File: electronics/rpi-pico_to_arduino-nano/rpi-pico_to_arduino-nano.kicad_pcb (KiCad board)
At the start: 2 copper layers, 2 parts, among them U1 Pico

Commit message: add some connections and comments
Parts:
- moved U1 2.62 mm to (153.7, 107.3)
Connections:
- A1 pad 1: unconnected-(A1-Pad1) -> /GPIO1
- A1 pad 10: unconnected-(A1-Pad10) -> /GPIO7
- A1 pad 11: unconnected-(A1-Pad11) -> /GPIO8
- A1 pad 12: unconnected-(A1-Pad12) -> /GPIO9
- A1 pad 13: unconnected-(A1-Pad13) -> /GPIO10
- A1 pad 14: unconnected-(A1-Pad14) -> /GPIO11
- A1 pad 15: unconnected-(A1-Pad15) -> /GPIO12
- A1 pad 16: unconnected-(A1-Pad16) -> /GPIO13
- A1 pad 19: unconnected-(A1-Pad19) -> /GPIO26_ADC0
- A1 pad 2: unconnected-(A1-Pad2) -> /GPIO0
- A1 pad 20: unconnected-(A1-Pad20) -> /GPIO27_ADC1
- A1 pad 21: unconnected-(A1-Pad21) -> /GPIO26_ADC0
- A1 pad 29: unconnected-(A1-Pad29) -> GND
- A1 pad 4: unconnected-(A1-Pad4) -> GND
- A1 pad 5: unconnected-(A1-Pad5) -> /GPIO2
- A1 pad 6: unconnected-(A1-Pad6) -> /GPIO3
- A1 pad 7: unconnected-(A1-Pad7) -> /GPIO4
- A1 pad 8: unconnected-(A1-Pad8) -> /GPIO5
- A1 pad 9: unconnected-(A1-Pad9) -> /GPIO6
- U1 pad 1: unconnected-(U1-Pad1) -> /GPIO0
- U1 pad 10: unconnected-(U1-Pad10) -> /GPIO7
- U1 pad 11: unconnected-(U1-Pad11) -> /GPIO8
- U1 pad 12: unconnected-(U1-Pad12) -> /GPIO9
- U1 pad 13: unconnected-(U1-Pad13) -> GND
- U1 pad 14: unconnected-(U1-Pad14) -> /GPIO10
- U1 pad 15: unconnected-(U1-Pad15) -> /GPIO11
- U1 pad 16: unconnected-(U1-Pad16) -> /GPIO12
- U1 pad 17: unconnected-(U1-Pad17) -> /GPIO13
- U1 pad 18: unconnected-(U1-Pad18) -> GND
- U1 pad 19: unconnected-(U1-Pad19) -> /GPIO14
- U1 pad 2: unconnected-(U1-Pad2) -> /GPIO1
- U1 pad 20: unconnected-(U1-Pad20) -> /GPIO15
- U1 pad 21: unconnected-(U1-Pad21) -> /GPIO16
- U1 pad 22: unconnected-(U1-Pad22) -> /GPIO17
- U1 pad 23: unconnected-(U1-Pad23) -> GND
- U1 pad 24: unconnected-(U1-Pad24) -> /GPIO18
- U1 pad 25: unconnected-(U1-Pad25) -> /GPIO19
- U1 pad 26: unconnected-(U1-Pad26) -> /GPIO20
- U1 pad 27: unconnected-(U1-Pad27) -> /GPIO21
- U1 pad 28: unconnected-(U1-Pad28) -> GND
- U1 pad 29: unconnected-(U1-Pad29) -> /GPIO22
- U1 pad 3: unconnected-(U1-Pad3) -> GND
- U1 pad 30: unconnected-(U1-Pad30) -> /RUN
- U1 pad 31: unconnected-(U1-Pad31) -> /GPIO26_ADC0
- U1 pad 32: unconnected-(U1-Pad32) -> /GPIO27_ADC1
- U1 pad 33: unconnected-(U1-Pad33) -> GND
- U1 pad 34: unconnected-(U1-Pad34) -> /GPIO28_ADC2
- U1 pad 35: unconnected-(U1-Pad35) -> /ADC_VREF
- U1 pad 36: unconnected-(U1-Pad36) -> /3V3
- U1 pad 37: unconnected-(U1-Pad37) -> /3V3_EN
- U1 pad 38: unconnected-(U1-Pad38) -> GND
- U1 pad 39: unconnected-(U1-Pad39) -> /VSYS
- U1 pad 4: unconnected-(U1-Pad4) -> /GPIO2
- U1 pad 40: unconnected-(U1-Pad40) -> /VBUS
- U1 pad 41: unconnected-(U1-Pad41) -> /SWCLK
- U1 pad 42: unconnected-(U1-Pad42) -> GND
- U1 pad 43: unconnected-(U1-Pad43) -> /SWDIO
- U1 pad 5: unconnected-(U1-Pad5) -> /GPIO3
- U1 pad 6: unconnected-(U1-Pad6) -> /GPIO4
- U1 pad 7: unconnected-(U1-Pad7) -> /GPIO5
- U1 pad 8: unconnected-(U1-Pad8) -> GND
- U1 pad 9: unconnected-(U1-Pad9) -> /GPIO6

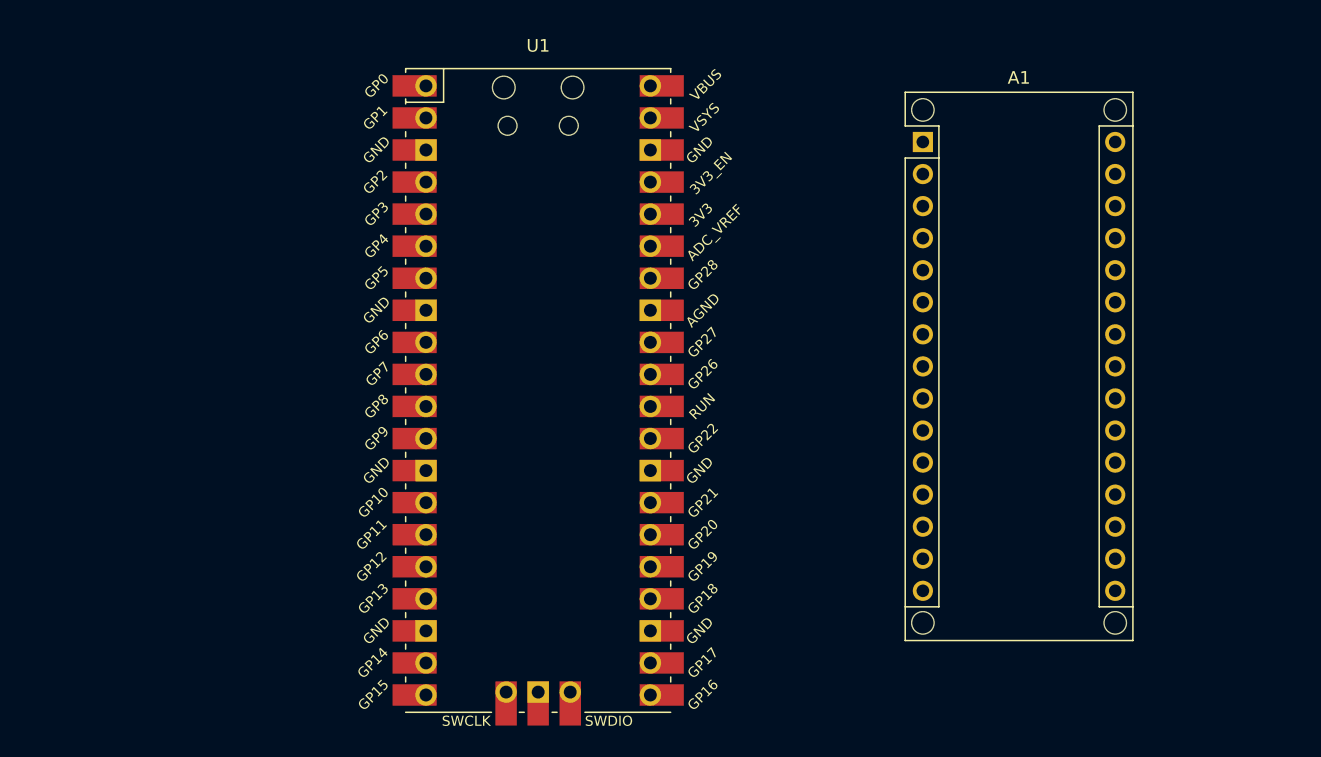
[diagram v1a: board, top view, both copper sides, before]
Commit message: add connection matrix
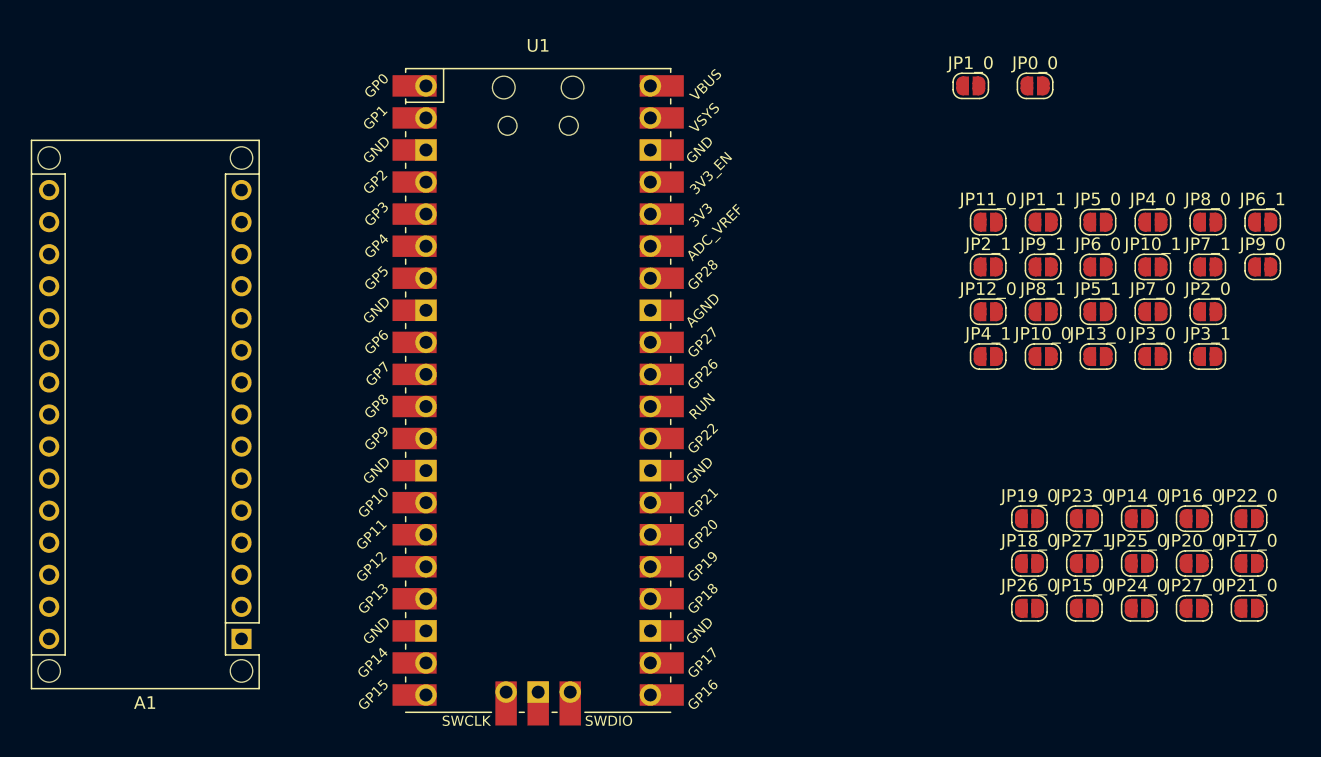
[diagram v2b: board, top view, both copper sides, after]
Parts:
- added JP0_0: SolderJumper_2_Open, Jumper:SolderJumper-2_P1.3mm_Open_RoundedPad1.0x1.5mm, F.Cu at (193.0, 83.2)
- added JP10_0: SolderJumper_2_Open, Jumper:SolderJumper-2_P1.3mm_Open_RoundedPad1.0x1.5mm, F.Cu at (193.7, 104.6)
- added JP10_1: SolderJumper_2_Open, Jumper:SolderJumper-2_P1.3mm_Open_RoundedPad1.0x1.5mm, F.Cu at (202.4, 97.5)
- added JP11_0: SolderJumper_2_Open, Jumper:SolderJumper-2_P1.3mm_Open_RoundedPad1.0x1.5mm, F.Cu at (189.3, 94.0)
- added JP12_0: SolderJumper_2_Open, Jumper:SolderJumper-2_P1.3mm_Open_RoundedPad1.0x1.5mm, F.Cu at (189.3, 101.1)
- added JP13_0: SolderJumper_2_Open, Jumper:SolderJumper-2_P1.3mm_Open_RoundedPad1.0x1.5mm, F.Cu at (198.0, 104.6)
- added JP14_0: SolderJumper_2_Open, Jumper:SolderJumper-2_P1.3mm_Open_RoundedPad1.0x1.5mm, F.Cu at (201.3, 117.5)
- added JP15_0: SolderJumper_2_Open, Jumper:SolderJumper-2_P1.3mm_Open_RoundedPad1.0x1.5mm, F.Cu at (196.9, 124.6)
- added JP16_0: SolderJumper_2_Open, Jumper:SolderJumper-2_P1.3mm_Open_RoundedPad1.0x1.5mm, F.Cu at (205.6, 117.5)
- added JP17_0: SolderJumper_2_Open, Jumper:SolderJumper-2_P1.3mm_Open_RoundedPad1.0x1.5mm, F.Cu at (210.0, 121.0)
- added JP18_0: SolderJumper_2_Open, Jumper:SolderJumper-2_P1.3mm_Open_RoundedPad1.0x1.5mm, F.Cu at (192.6, 121.0)
- added JP19_0: SolderJumper_2_Open, Jumper:SolderJumper-2_P1.3mm_Open_RoundedPad1.0x1.5mm, F.Cu at (192.6, 117.5)
- added JP1_0: SolderJumper_2_Open, Jumper:SolderJumper-2_P1.3mm_Open_RoundedPad1.0x1.5mm, F.Cu at (187.9, 83.2)
- added JP1_1: SolderJumper_2_Open, Jumper:SolderJumper-2_P1.3mm_Open_RoundedPad1.0x1.5mm, F.Cu at (193.7, 94.0)
- added JP20_0: SolderJumper_2_Open, Jumper:SolderJumper-2_P1.3mm_Open_RoundedPad1.0x1.5mm, F.Cu at (205.6, 121.0)
- added JP21_0: SolderJumper_2_Open, Jumper:SolderJumper-2_P1.3mm_Open_RoundedPad1.0x1.5mm, F.Cu at (210.0, 124.6)
- added JP22_0: SolderJumper_2_Open, Jumper:SolderJumper-2_P1.3mm_Open_RoundedPad1.0x1.5mm, F.Cu at (210.0, 117.5)
- added JP23_0: SolderJumper_2_Open, Jumper:SolderJumper-2_P1.3mm_Open_RoundedPad1.0x1.5mm, F.Cu at (196.9, 117.5)
- added JP24_0: SolderJumper_2_Open, Jumper:SolderJumper-2_P1.3mm_Open_RoundedPad1.0x1.5mm, F.Cu at (201.3, 124.6)
- added JP25_0: SolderJumper_2_Open, Jumper:SolderJumper-2_P1.3mm_Open_RoundedPad1.0x1.5mm, F.Cu at (201.3, 121.0)
- added JP26_0: SolderJumper_2_Open, Jumper:SolderJumper-2_P1.3mm_Open_RoundedPad1.0x1.5mm, F.Cu at (192.6, 124.6)
- added JP27_0: SolderJumper_2_Open, Jumper:SolderJumper-2_P1.3mm_Open_RoundedPad1.0x1.5mm, F.Cu at (205.6, 124.6)
- added JP27_1: SolderJumper_2_Open, Jumper:SolderJumper-2_P1.3mm_Open_RoundedPad1.0x1.5mm, F.Cu at (196.9, 121.0)
- added JP2_0: SolderJumper_2_Open, Jumper:SolderJumper-2_P1.3mm_Open_RoundedPad1.0x1.5mm, F.Cu at (206.7, 101.1)
- added JP2_1: SolderJumper_2_Open, Jumper:SolderJumper-2_P1.3mm_Open_RoundedPad1.0x1.5mm, F.Cu at (189.3, 97.5)
- added JP3_0: SolderJumper_2_Open, Jumper:SolderJumper-2_P1.3mm_Open_RoundedPad1.0x1.5mm, F.Cu at (202.4, 104.6)
- added JP3_1: SolderJumper_2_Open, Jumper:SolderJumper-2_P1.3mm_Open_RoundedPad1.0x1.5mm, F.Cu at (206.7, 104.6)
- added JP4_0: SolderJumper_2_Open, Jumper:SolderJumper-2_P1.3mm_Open_RoundedPad1.0x1.5mm, F.Cu at (202.4, 94.0)
- added JP4_1: SolderJumper_2_Open, Jumper:SolderJumper-2_P1.3mm_Open_RoundedPad1.0x1.5mm, F.Cu at (189.3, 104.6)
- added JP5_0: SolderJumper_2_Open, Jumper:SolderJumper-2_P1.3mm_Open_RoundedPad1.0x1.5mm, F.Cu at (198.0, 94.0)
- added JP5_1: SolderJumper_2_Open, Jumper:SolderJumper-2_P1.3mm_Open_RoundedPad1.0x1.5mm, F.Cu at (198.0, 101.1)
- added JP6_0: SolderJumper_2_Open, Jumper:SolderJumper-2_P1.3mm_Open_RoundedPad1.0x1.5mm, F.Cu at (198.0, 97.5)
- added JP6_1: SolderJumper_2_Open, Jumper:SolderJumper-2_P1.3mm_Open_RoundedPad1.0x1.5mm, F.Cu at (211.1, 94.0)
- added JP7_0: SolderJumper_2_Open, Jumper:SolderJumper-2_P1.3mm_Open_RoundedPad1.0x1.5mm, F.Cu at (202.4, 101.1)
- added JP7_1: SolderJumper_2_Open, Jumper:SolderJumper-2_P1.3mm_Open_RoundedPad1.0x1.5mm, F.Cu at (206.7, 97.5)
- added JP8_0: SolderJumper_2_Open, Jumper:SolderJumper-2_P1.3mm_Open_RoundedPad1.0x1.5mm, F.Cu at (206.7, 94.0)
- added JP8_1: SolderJumper_2_Open, Jumper:SolderJumper-2_P1.3mm_Open_RoundedPad1.0x1.5mm, F.Cu at (193.7, 101.1)
- added JP9_0: SolderJumper_2_Open, Jumper:SolderJumper-2_P1.3mm_Open_RoundedPad1.0x1.5mm, F.Cu at (211.1, 97.5)
- added JP9_1: SolderJumper_2_Open, Jumper:SolderJumper-2_P1.3mm_Open_RoundedPad1.0x1.5mm, F.Cu at (193.7, 97.5)
- moved A1 66.8 mm to (130.2, 127.0), turned to 180 degrees
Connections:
- A1 pad 1: /GPIO1 -> /D1/TX
- A1 pad 10: /GPIO7 -> /D7
- A1 pad 11: /GPIO8 -> /D8
- A1 pad 12: /GPIO9 -> /D9
- A1 pad 13: /GPIO10 -> /D10
- A1 pad 14: /GPIO11 -> /D11
- A1 pad 15: /GPIO12 -> /D12
- A1 pad 16: /GPIO13 -> /D13
- A1 pad 17: unconnected-(A1-Pad17) -> /3V3
- A1 pad 18: unconnected-(A1-Pad18) -> /AREF
- A1 pad 19: /GPIO26_ADC0 -> /A0
- A1 pad 2: /GPIO0 -> /DO/RX
- A1 pad 20: /GPIO27_ADC1 -> /A1
- A1 pad 21: /GPIO26_ADC0 -> /A2
- A1 pad 22: unconnected-(A1-Pad22) -> /A3
- A1 pad 23: unconnected-(A1-Pad23) -> /A4
- A1 pad 24: unconnected-(A1-Pad24) -> /A5
- A1 pad 25: unconnected-(A1-Pad25) -> /A6
- A1 pad 26: unconnected-(A1-Pad26) -> /A7
- A1 pad 27: unconnected-(A1-Pad27) -> /+5V
- A1 pad 28: unconnected-(A1-Pad28) -> /~{RESET}
- A1 pad 3: unconnected-(A1-Pad3) -> /~{RESET}
- A1 pad 30: unconnected-(A1-Pad30) -> /VIN
- A1 pad 5: /GPIO2 -> /D2
- A1 pad 6: /GPIO3 -> /D3
- A1 pad 7: /GPIO4 -> /D4
- A1 pad 8: /GPIO5 -> /D5
- A1 pad 9: /GPIO6 -> /D6
- U1 pad 33: GND -> /AGND
- U1 pad 37: /3V3_EN -> unconnected-(U1-Pad37)

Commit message: place components on pcb
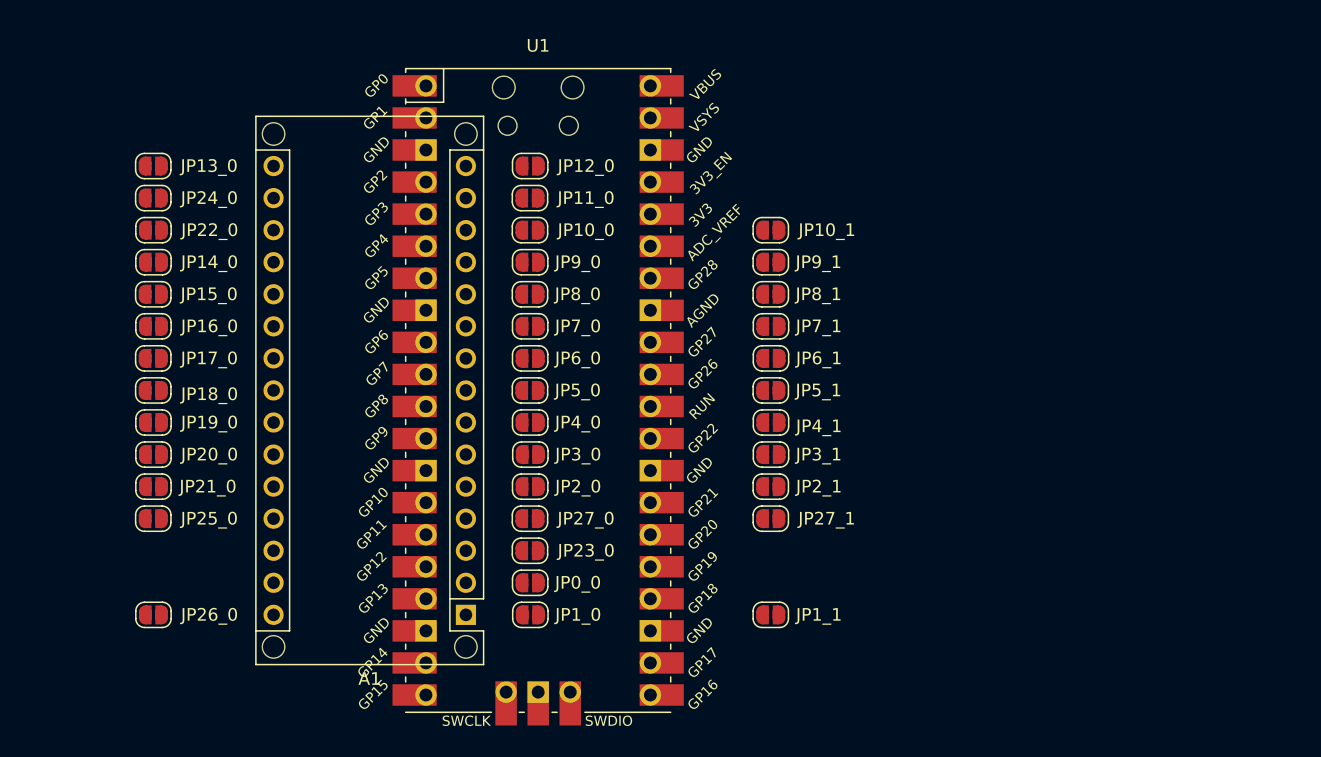
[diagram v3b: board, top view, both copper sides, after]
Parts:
- moved JP22_0 89.8 mm to (123.2, 94.6), turned to 180 degrees
- moved JP17_0 88.3 mm to (123.2, 104.8), turned to 180 degrees
- moved JP21_0 87.3 mm to (123.2, 114.9), turned to 180 degrees
- moved JP24_0 84.6 mm to (123.2, 92.1), turned to 180 degrees
- moved JP16_0 83.9 mm to (123.2, 102.2), turned to 180 degrees
- moved JP20_0 82.9 mm to (123.2, 112.4), turned to 180 degrees
- moved JP14_0 80.7 mm to (123.2, 97.2), turned to 180 degrees
- moved JP25_0 78.2 mm to (123.2, 117.5), turned to 180 degrees
- moved JP15_0 77.9 mm to (123.2, 99.7), turned to 180 degrees
- moved JP13_0 76.4 mm to (123.2, 89.5), turned to 180 degrees
- moved JP18_0 70.8 mm to (123.2, 107.3), turned to 180 degrees
- moved JP19_0 69.8 mm to (123.2, 109.9), turned to 180 degrees
- moved JP26_0 69.4 mm to (123.2, 125.1), turned to 180 degrees
- moved JP9_0 58.0 mm to (153.0, 97.2)
- moved JP0_0 56.1 mm to (153.0, 122.6)
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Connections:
- JP17_0 pad 2: unconnected-(JP17_0-Pad2) -> /GPIO22
- JP24_0 pad 2: /3V3 -> /3V3_pico
- JP27_0 pad 2: GND -> /GND_pico
- U1 pad 13: GND -> /GND_pico
- U1 pad 18: GND -> /GND_pico
- U1 pad 23: GND -> /GND_pico
- U1 pad 28: GND -> /GND_pico
- U1 pad 3: GND -> /GND_pico
- U1 pad 36: /3V3 -> /3V3_pico
- U1 pad 38: GND -> /GND_pico
- U1 pad 41: /SWCLK -> unconnected-(U1-Pad41)
- U1 pad 42: GND -> /GND_pico
- U1 pad 43: /SWDIO -> unconnected-(U1-Pad43)
- U1 pad 8: GND -> /GND_pico

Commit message: default closed solder jumpers, datasheets, erc
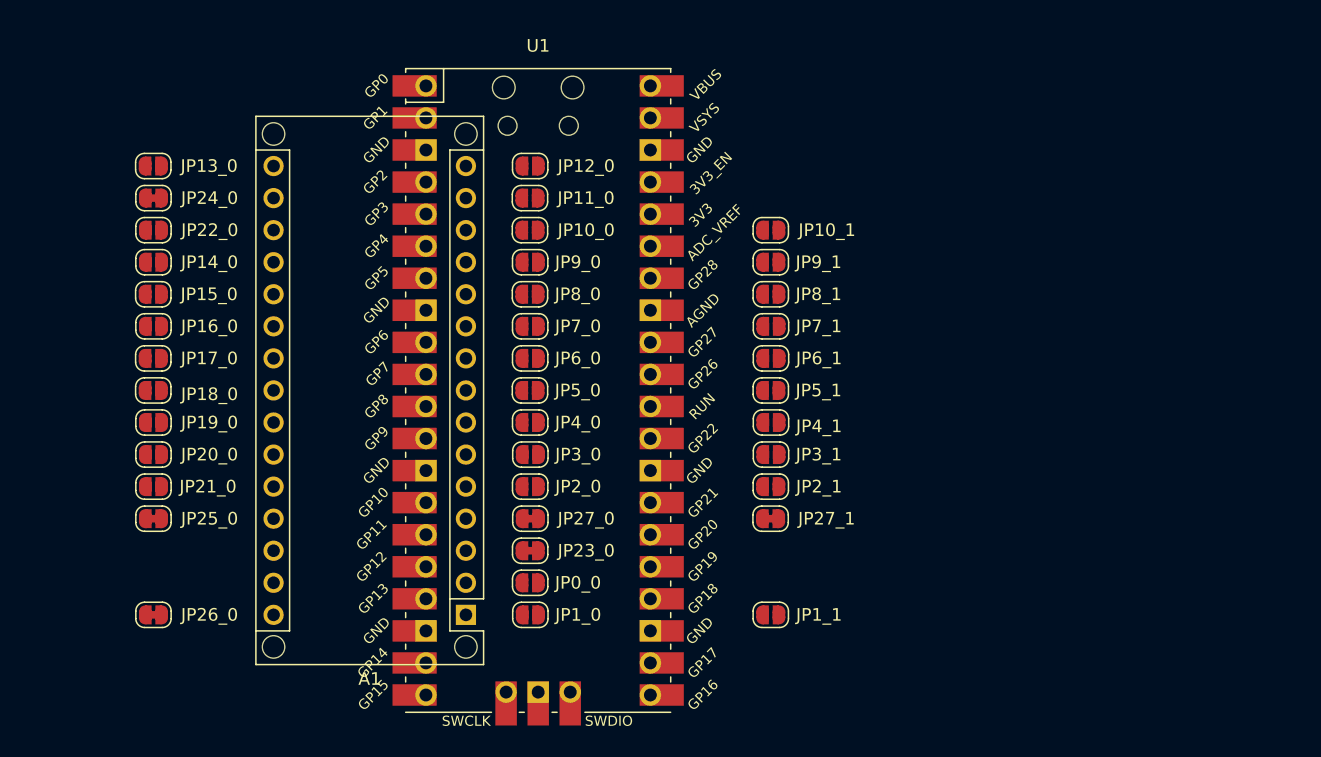
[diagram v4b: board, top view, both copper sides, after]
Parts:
- JP23_0, JP24_0, JP25_0, JP26_0, JP27_0, JP27_1: value SolderJumper_2_Open -> SolderJumper_2_Bridged; footprint Jumper:SolderJumper-2_P1.3mm_Open_RoundedPad1.0x1.5mm -> Jumper:SolderJumper-2_P1.3mm_Bridged_RoundedPad1.0x1.5mm

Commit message: route pcb
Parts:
- JP0_0, JP10_0, JP10_1, JP11_0, JP12_0, JP13_0, JP14_0, JP15_0, JP16_0, JP17_0, JP18_0, JP19_0, JP1_0, JP1_1, JP20_0, JP21_0, JP22_0, JP23_0, JP24_0, JP25_0, JP26_0, JP27_0, JP27_1, JP2_0, JP2_1, JP3_0, JP3_1, JP4_0, JP4_1, JP5_0, JP5_1, JP6_0, JP6_1, JP7_0, JP7_1, JP8_0, JP8_1, JP9_0, JP9_1: moved to B.Cu
- moved JP15_0 12.7 mm to (135.9, 99.7), turned to 0 degrees
- moved JP17_0 12.7 mm to (135.9, 104.8), turned to 0 degrees
- moved JP18_0 12.7 mm to (135.9, 107.3), turned to 0 degrees
- moved JP13_0 12.7 mm to (135.9, 89.5), turned to 0 degrees
- moved JP14_0 12.7 mm to (135.9, 97.2), turned to 0 degrees
- moved JP16_0 12.7 mm to (135.9, 102.2), turned to 0 degrees
- moved JP19_0 12.7 mm to (135.9, 109.9), turned to 0 degrees
- moved JP20_0 12.7 mm to (135.9, 112.4), turned to 0 degrees
- moved JP21_0 12.7 mm to (135.9, 114.9), turned to 0 degrees
- moved JP22_0 12.7 mm to (135.9, 94.6), turned to 0 degrees
- moved JP24_0 12.7 mm to (135.9, 92.1), turned to 0 degrees
- moved JP25_0 12.7 mm to (135.9, 117.5), turned to 0 degrees
- moved JP26_0 12.7 mm to (135.9, 125.1), turned to 0 degrees
- moved JP3_1 6.40 mm to (165.7, 112.4)
- moved JP4_1 6.40 mm to (165.7, 109.9)
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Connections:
- net /DO/RX renamed /D0/RX
- A1 pad 28: /~{RESET} -> unconnected-(A1-Pad28)
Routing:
- net /GND_pico: track 0.00 -> 131.6 mm, vias 0 -> 4
- net /GPIO13: track 0.00 -> 111.6 mm, vias 0 -> 3
- net /VSYS: track 0.00 -> 101.0 mm
- net /VBUS: track 0.00 -> 81.5 mm, vias 0 -> 2
- net /GPIO15: track 0.00 -> 63.5 mm, vias 0 -> 2
- net /GPIO1: track 0.00 -> 60.4 mm, vias 0 -> 2
- net /GPIO0: track 0.00 -> 59.8 mm, vias 0 -> 2
- net /GPIO14: track 0.00 -> 58.9 mm, vias 0 -> 2
- net /GPIO12: track 0.00 -> 50.4 mm, vias 0 -> 1
- net /GPIO2: track 0.00 -> 45.0 mm, vias 0 -> 1
- net /GPIO11: track 0.00 -> 44.0 mm, vias 0 -> 1
- net /GPIO28_ADC2: track 0.00 -> 39.9 mm, vias 0 -> 1
- net /GPIO3: track 0.00 -> 38.6 mm, vias 0 -> 1
- net /GPIO10: track 0.00 -> 37.7 mm, vias 0 -> 1
- net GND: track 0.00 -> 34.5 mm, vias 0 -> 2
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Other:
- board outline added: 41.9 x 52.7 mm
- board text added: "TODOs: - Füllflächen"
